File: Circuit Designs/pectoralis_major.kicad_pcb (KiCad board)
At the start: 4 copper layers, 100 x 100 mm, 293 parts, among them J1 0524651671, J2 0533071071, J3 0533071071, J4 0524651071, J5 SoicBite, Q1 AO3400A, Q2 AO3400A, Q3 BUK7V4R2, Q4 BUK7V4R2, Q5 BUK7V4R2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

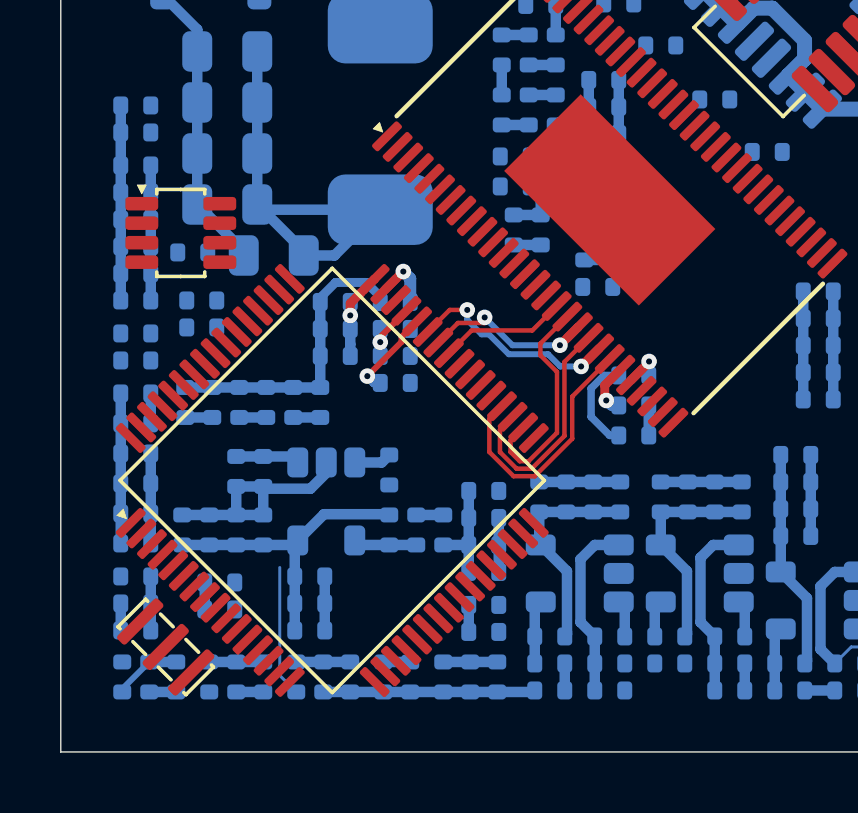
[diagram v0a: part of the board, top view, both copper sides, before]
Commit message: done the connection between the MCU and the motor driver
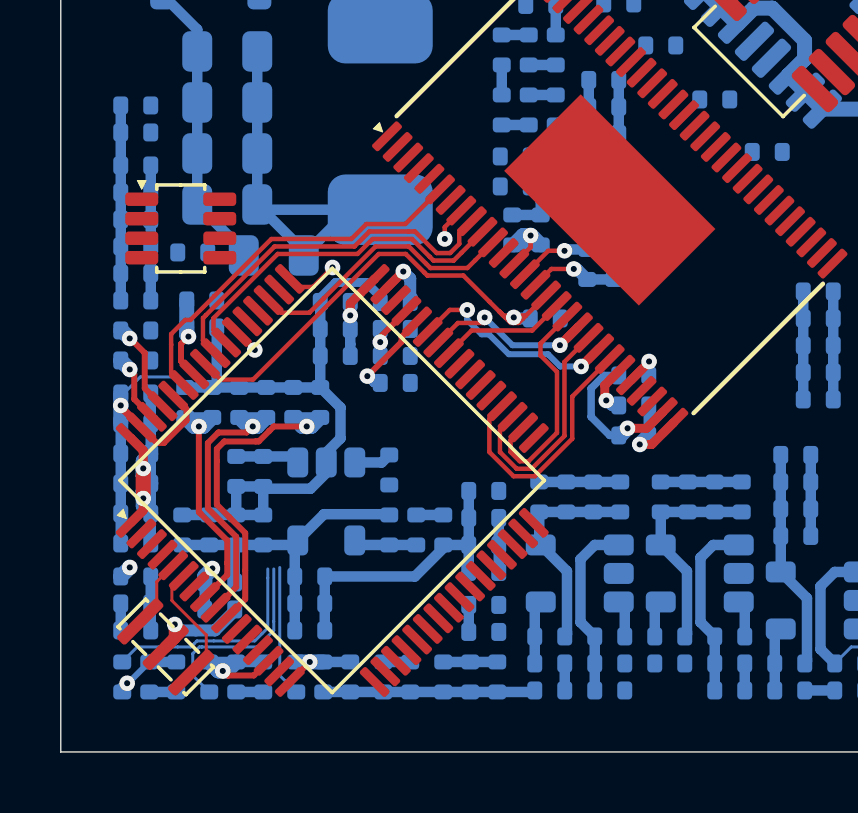
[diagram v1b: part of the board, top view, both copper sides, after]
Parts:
- moved R57 2.04 mm to (116.2, 135.6)
- moved C98 0.66 mm to (118.5, 133.8)
- moved C97 0.66 mm to (117.5, 133.8)
- moved U1 0.15 mm to (104.0, 132.6)
- moved R2 0.10 mm to (102.5, 135.9)
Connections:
- R10 pad 1: +3V3 -> +3.3VA
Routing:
- net GND: track 281.5 -> 303.7 mm, vias 45 -> 48
- net /powerDrivers/EN_GATE: track 0.00 -> 17.0 mm, vias 0 -> 1
- net /powerDrivers/FAULT: track 0.00 -> 12.8 mm
- net /powerDrivers/SDI: track 0.00 -> 12.4 mm
- net /powerDrivers/SDO: track 0.00 -> 11.7 mm
- net /powerSemicons/CURR_C: track 0.90 -> 11.7 mm, vias 0 -> 1
- net /powerDrivers/SCK: track 0.00 -> 9.22 mm
- net /powerSemicons/CURR_B: track 0.90 -> 9.94 mm, vias 0 -> 1
- net +3V3: track 54.4 -> 62.0 mm, vias 1 -> 3
- net /powerSemicons/CURR_A: track 0.90 -> 8.44 mm, vias 0 -> 1
- net /powerDrivers/SH_B: track 1.97 -> 9.26 mm
- net /powerDrivers/SH_A: track 2.86 -> 9.43 mm
- net Net-(U2-Pad6): track 0.00 -> 4.06 mm
- net /communication/CANRX: track 0.00 -> 3.13 mm, vias 0 -> 1
- net /powerDrivers/SENS_A: track 1.80 -> 4.74 mm, vias 0 -> 1
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
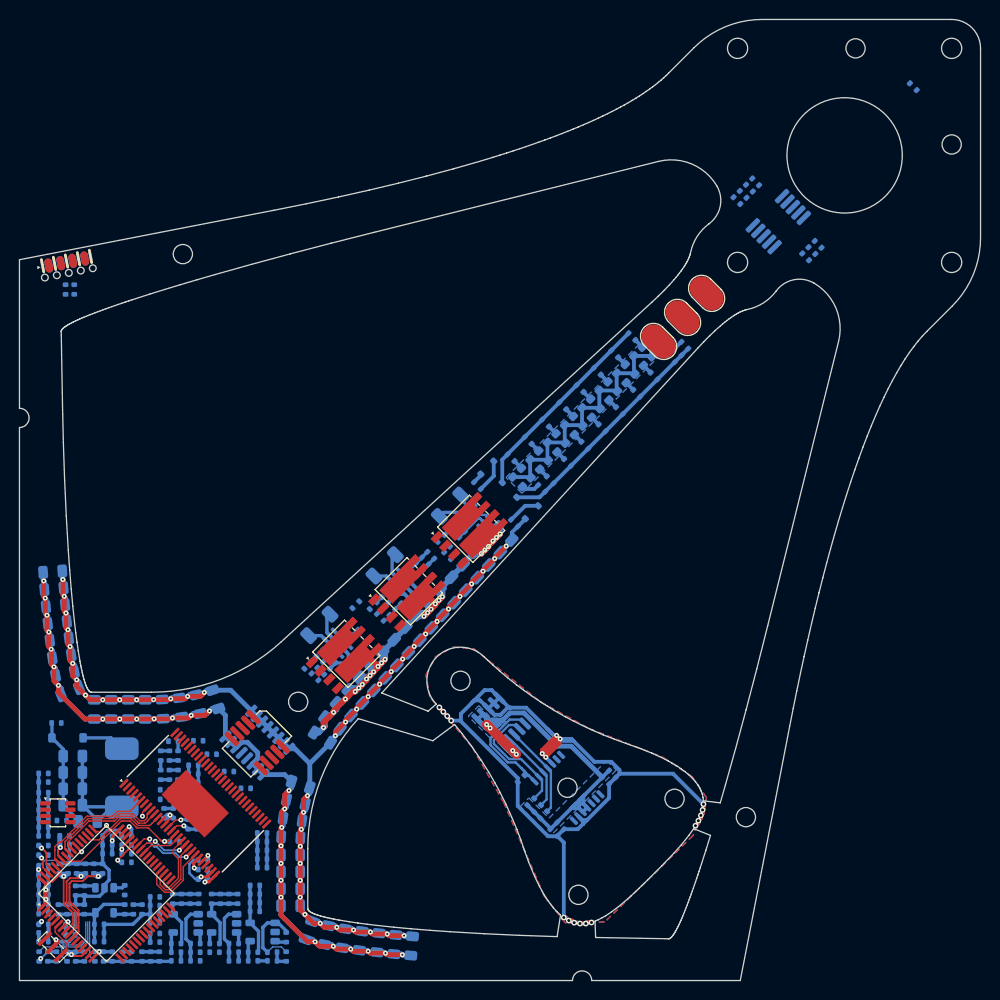
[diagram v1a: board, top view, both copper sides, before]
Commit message: done all the tracing between the driver and the mosfets
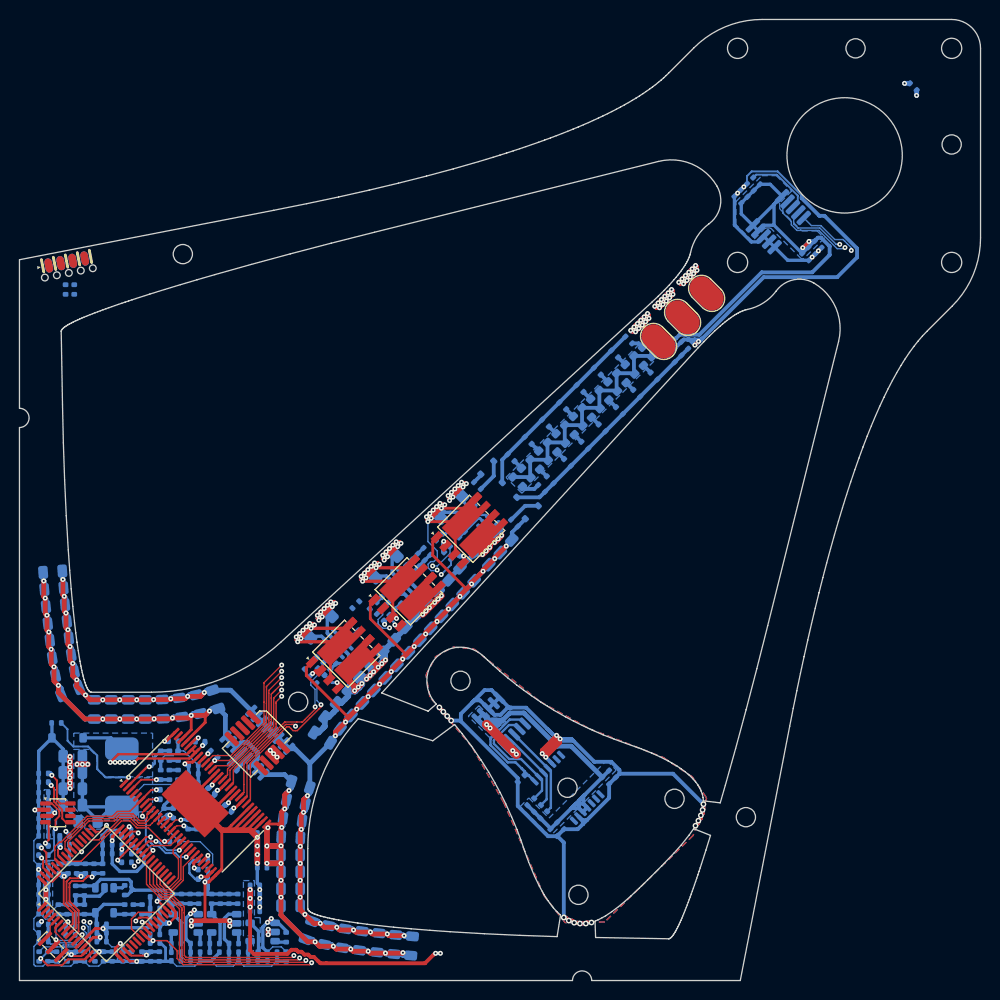
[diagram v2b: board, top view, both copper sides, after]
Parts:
- moved R3 18.7 mm to (122.2, 127.8), turned to -45 degrees
- moved SP1 7.07 mm to (166.5, 83.5)
- moved SP3 7.07 mm to (171.5, 78.5)
- moved R11 2.90 mm to (176.7, 66.8)
- moved C105 2.80 mm to (120.0, 130.3), turned to -45 degrees
- moved C110 2.80 mm to (121.7, 132.1), turned to -45 degrees
- moved C23 0.78 mm to (174.8, 68.8)
- moved C21 0.78 mm to (176.1, 67.5)
- moved C22 0.78 mm to (175.4, 68.1)
- moved C149 0.57 mm to (142.4, 105.3)
- moved C140 0.57 mm to (140.6, 107.1)
- moved C141 0.57 mm to (141.2, 106.5)
- moved C148 0.57 mm to (141.8, 105.9)
- moved R16 0.48 mm to (163.4, 83.3)
- moved C117 0.46 mm to (146.6, 107.7)
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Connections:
- R14 pad 1: +3.3VA -> +3V3
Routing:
- net GND: track 303.7 -> 535.8 mm, vias 48 -> 78
- net +3V3: track 62.0 -> 276.7 mm, vias 3 -> 14
- net /powerSemicons/PH_A: track 1.71 -> 162.2 mm, vias 0 -> 20
- net Net-(C55-Pad1): track 0.90 -> 156.1 mm, vias 0 -> 3
- net /powerSemicons/PH_C: track 2.51 -> 154.4 mm, vias 0 -> 20
- net /uController/ENC_MISO: track 0.00 -> 151.8 mm, vias 0 -> 2
- net /uController/ENC_nCS: track 0.00 -> 149.7 mm, vias 0 -> 2
- net /uController/ENC_SCK: track 0.00 -> 148.4 mm, vias 0 -> 2
- net /powerSemicons/PH_B: track 2.52 -> 127.4 mm, vias 0 -> 20
- net /powerDrivers/SH_A: track 9.43 -> 97.9 mm, vias 0 -> 13
- net +5V: track 29.1 -> 114.7 mm, vias 0 -> 10
- net /powerDrivers/SH_B: track 9.26 -> 76.3 mm, vias 0 -> 13
- net /powerDrivers/SH_C: track 6.35 -> 61.4 mm, vias 0 -> 12
- net /powerDrivers/GH_A: track 0.00 -> 39.3 mm, vias 0 -> 2
- net /powerDrivers/GL_A: track 0.00 -> 37.6 mm, vias 0 -> 2
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- added copper zone on In1.Cu, net +3V3
- added copper zone on B.Cu, net +5V
- added copper zone on In1.Cu, net /powerDrivers/SH_A
- added copper zone on In2.Cu, net /powerDrivers/SH_A
- added copper zone on In1.Cu, net /powerDrivers/SH_B
- added copper zone on In2.Cu, net /powerDrivers/SH_B
- added copper zone on In1.Cu, net /powerDrivers/SH_C
- added copper zone on In2.Cu, net /powerDrivers/SH_C
- added copper zone on In1.Cu, net /powerSemicons/PH_A
- added copper zone on In2.Cu, net /powerSemicons/PH_A
- added copper zone on In1.Cu, net /powerSemicons/PH_B
- added copper zone on In2.Cu, net /powerSemicons/PH_B
- added copper zone on In1.Cu, net /powerSemicons/PH_C
- added copper zone on In2.Cu, net /powerSemicons/PH_C
- added copper zone on In1.Cu, net GND
- added copper zone on In2.Cu, net GND
- added copper zone on B.Cu, net Net-(C91-Pad2)

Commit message: done mosfet tracing
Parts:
- moved T2 7.45 mm to (129.5, 115.9), turned to 0 degrees
- moved R34 3.25 mm to (150.7, 99.2), turned to -135 degrees
- moved C149 2.15 mm to (140.8, 103.8), turned to 45 degrees
- moved C148 1.30 mm to (140.8, 105.0), turned to 45 degrees
- moved R16 0.91 mm to (163.2, 84.2), turned to -135 degrees
- moved R81 0.78 mm to (136.2, 110.5)
- moved R78 0.64 mm to (137.6, 109.3)
- moved R75 0.53 mm to (137.2, 112.6)
- moved C144 0.46 mm to (134.6, 114.1)
- moved R70 0.46 mm to (131.7, 118.2)
- moved R79 0.46 mm to (131.6, 116.3)
- moved R82 0.46 mm to (130.4, 117.6)
- moved C145 0.46 mm to (135.2, 113.5)
- moved U10 0.46 mm to (133.5, 115.3)
- moved C138 0.46 mm to (132.9, 117.0)
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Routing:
- net /powerSemicons/PH_C: track 154.4 -> 45.6 mm, vias 20 -> 21
- net +2V5: track 11.9 -> 60.8 mm, vias 0 -> 3
- net /uController/LED_RED: track 3.46 -> 37.1 mm
- net /powerSemicons/CURR_A: track 8.44 -> 32.7 mm, vias 1 -> 3
- net GND: track 535.8 -> 559.6 mm, vias 78 -> 86
- net +5VA: track 44.3 -> 67.5 mm
- net /powerSemicons/CURR_B: track 9.94 -> 24.3 mm
- net /powerSemicons/CURR_C: track 10.5 -> 16.7 mm
- net Net-(Q4-Pad2): track 0.00 -> 1.66 mm, vias 0 -> 1
- net /uController/LED_AMBER: track 4.51 -> 5.32 mm
- net Net-(Q2-Pad3): track 20.5 -> 19.9 mm
- net /powerDrivers/SH_A: track 97.9 -> 97.5 mm, vias 13 -> 14
